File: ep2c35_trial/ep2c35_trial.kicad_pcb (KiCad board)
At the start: 4 copper layers, 70.4 x 57.6 mm, 139 parts, among them J1 Conn_02x21_Odd_Even, J2 Conn_02x21_Odd_Even, J3 3M_8540-4500PL, J4 USB3_B_Micro_Amphenol_GSB343K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, J5 Conn_02x05_Odd_Even, J6 Conn_01x02_Male, J7 Conn_01x02_Male, J8 Conn_01x02_Male, J9 Conn_01x02_Male, U1 EP2C5F484, U2 MIC37302, U3 FT600Q-B-T, U4 W25Q16JVSNIQ, U5 MIC39102, U6 MIC49150-1.2, X1 FNETHE025, Y1 ABM7-30.000MHZ-D2Y-T

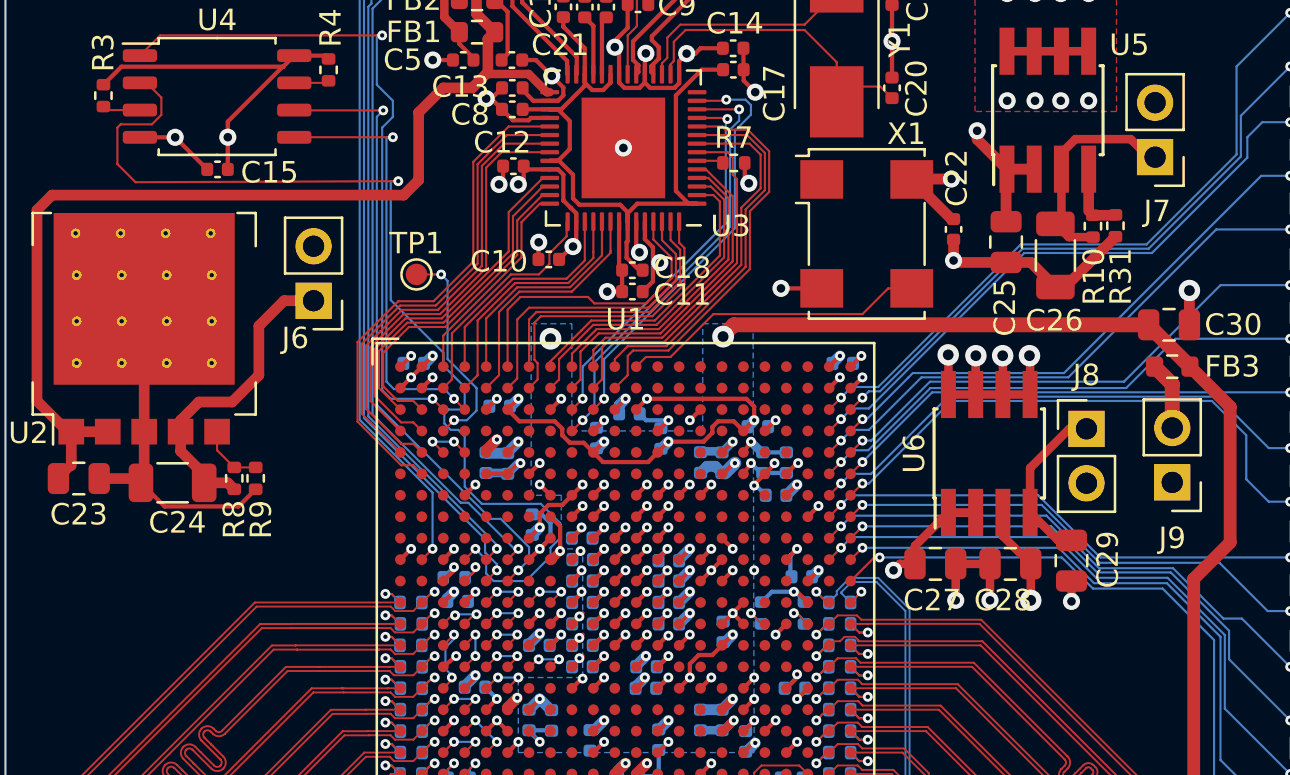
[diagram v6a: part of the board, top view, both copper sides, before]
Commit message: Create assembly file. WIP.
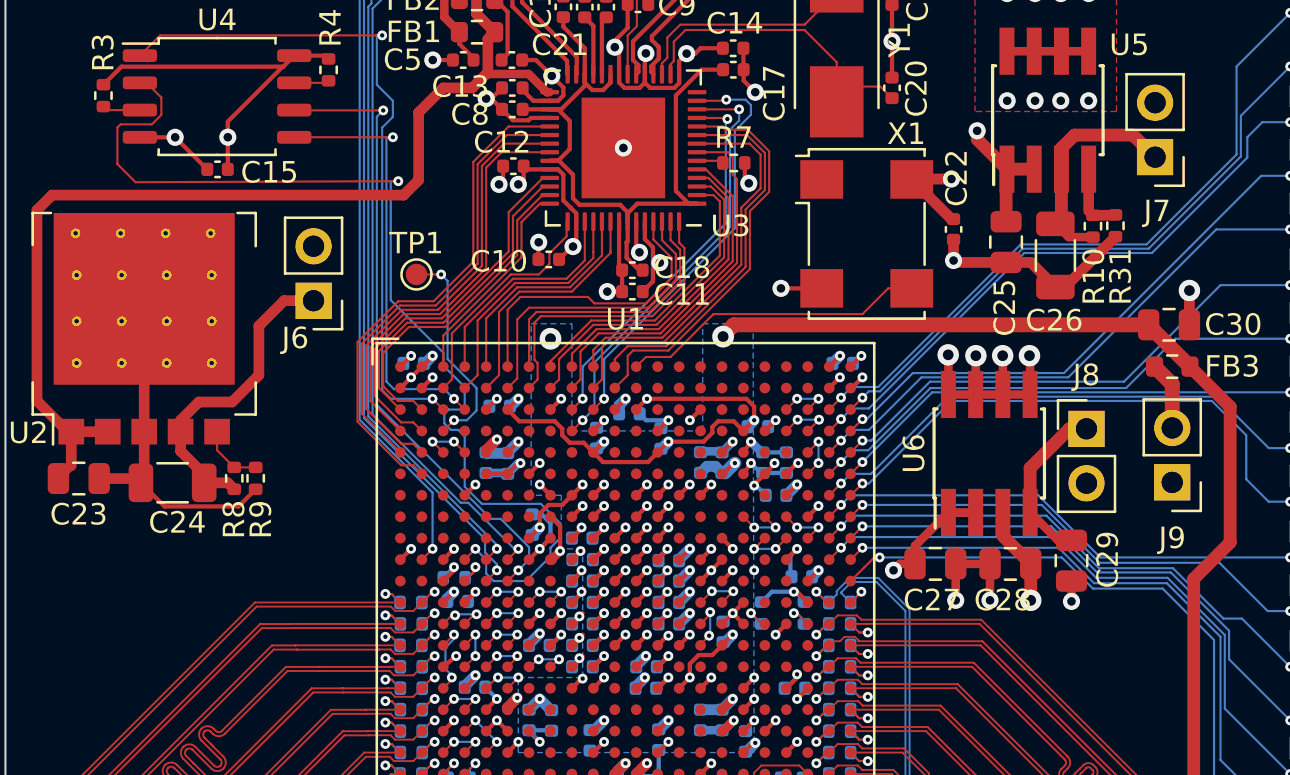
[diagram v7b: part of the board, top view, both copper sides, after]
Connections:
- U1 pad C19: unconnected-(U1-PadC19) -> /LVDS101
- U1 pad C20: unconnected-(U1-PadC20) -> /LVDS101
- U1 pad D19: unconnected-(U1-PadD19) -> /LVDS100
- U1 pad D20: unconnected-(U1-PadD20) -> /LVDS100
- U1 pad E20: unconnected-(U1-PadE20) -> /LVDS105
- U1 pad F20: unconnected-(U1-PadF20) -> /LVDS105
- U1 pad H17: unconnected-(U1-PadH17) -> /LVDS111
- U1 pad H18: unconnected-(U1-PadH18) -> /LVDS111
- U1 pad H19: unconnected-(U1-PadH19) -> /LVDS120
- U1 pad J18: unconnected-(U1-PadJ18) -> /LVDS117
- U1 pad J19: unconnected-(U1-PadJ19) -> /LVDS117
- U1 pad J20: unconnected-(U1-PadJ20) -> /LVDS120
- U1 pad M15: unconnected-(U1-PadM15) -> /LVDS130
- U1 pad M16: unconnected-(U1-PadM16) -> /LVDS130
- U1 pad N15: unconnected-(U1-PadN15) -> /LVDS132
- U1 pad P15: unconnected-(U1-PadP15) -> /LVDS132
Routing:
- net /LVDS105: track 0.00 -> 2.56 mm, vias 0 -> 2
- net /LVDS132: track 0.00 -> 2.54 mm, vias 0 -> 2
- net /LVDS130: track 0.00 -> 2.52 mm, vias 0 -> 2
- net /LVDS101: track 0.00 -> 2.51 mm, vias 0 -> 2
- net /LVDS100: track 0.00 -> 2.51 mm, vias 0 -> 2
- net /LVDS120: track 0.00 -> 2.48 mm, vias 0 -> 2
- net /LVDS117: track 0.00 -> 2.41 mm, vias 0 -> 2
- net /LVDS111: track 0.00 -> 2.41 mm, vias 0 -> 2
- net /2V5_LDO: track 10.1 -> 11.5 mm

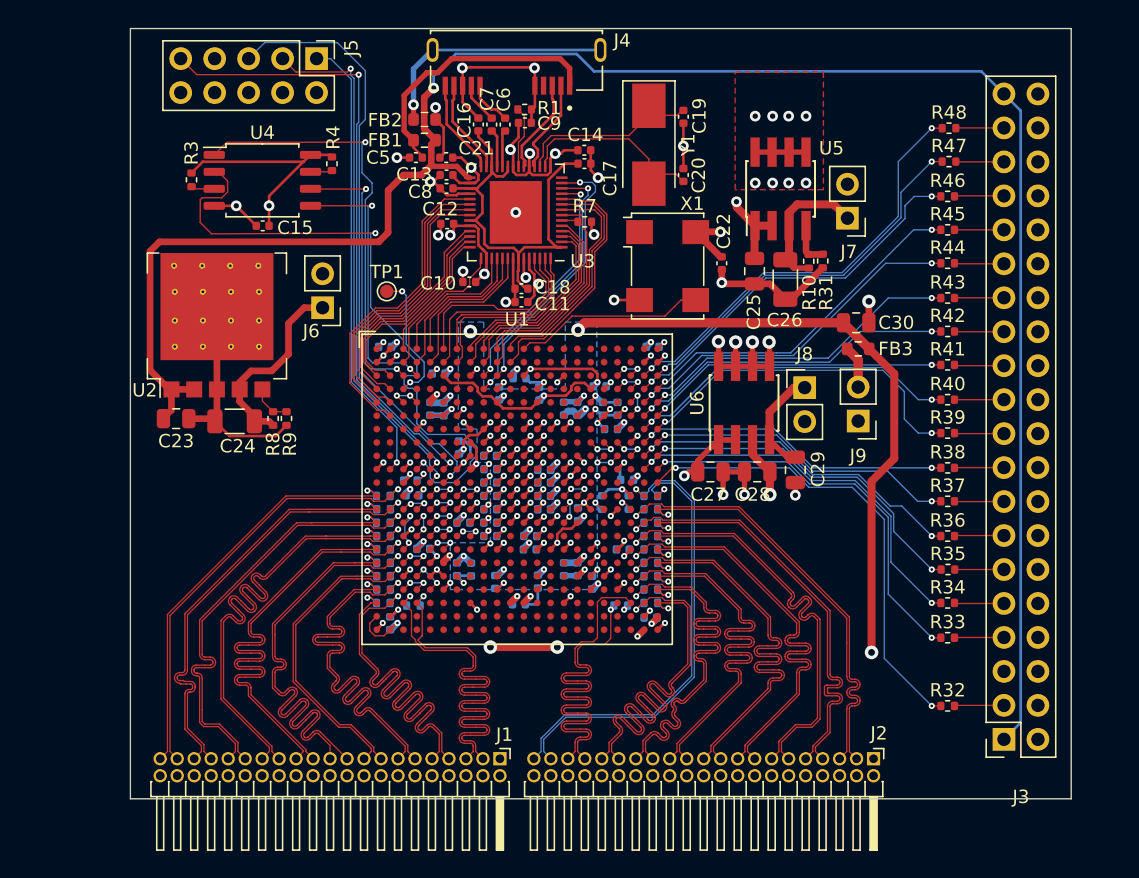
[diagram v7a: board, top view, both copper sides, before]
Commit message: Move JLCPCB components to bottom.
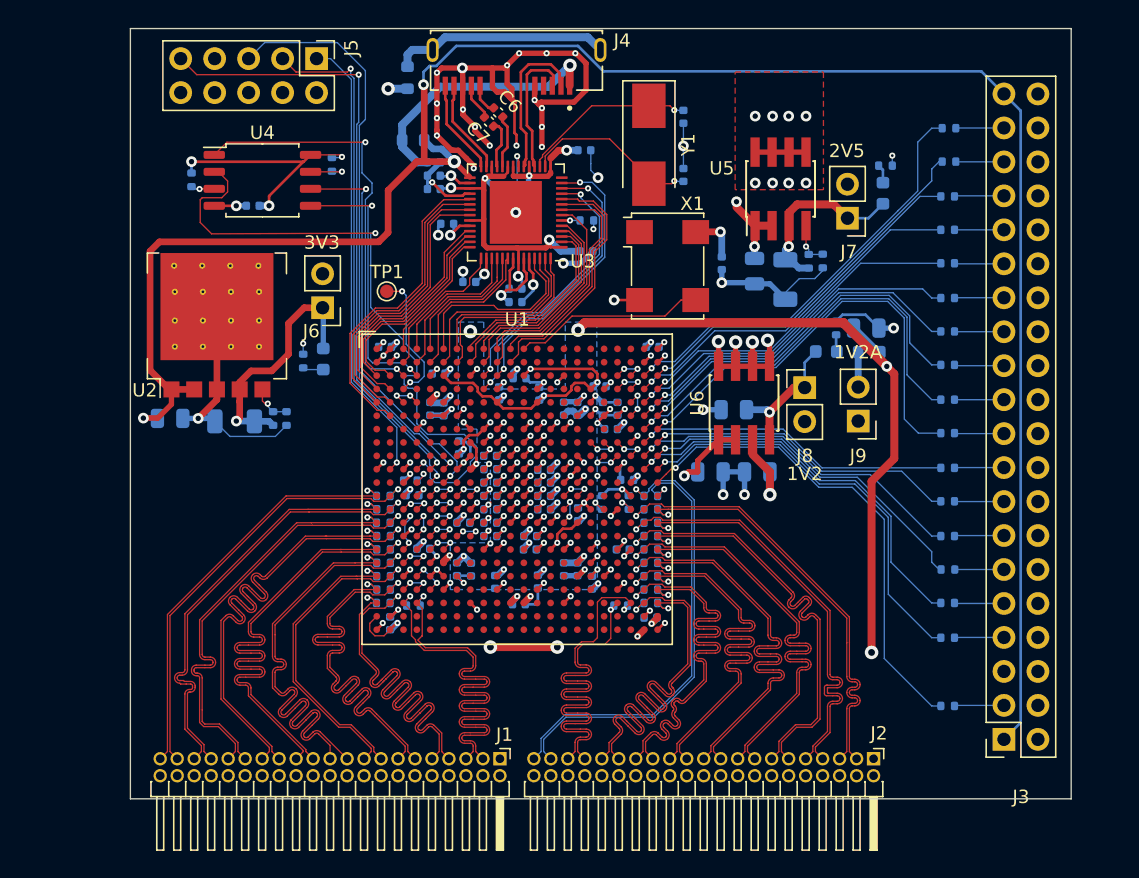
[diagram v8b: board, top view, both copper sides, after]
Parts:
- removed C21: 4.7u, Capacitor_SMD:C_0402_1005Metric
- added D1: LED, LED_SMD:LED_0603_1608Metric, B.Cu at (130.0, 71.8)
- added D2: LED, LED_SMD:LED_0603_1608Metric, B.Cu at (171.8, 59.4)
- added D3: LED, LED_SMD:LED_0603_1608Metric, B.Cu at (167.6, 71.2)
- added R49: 1k, Resistor_SMD:R_0402_1005Metric, B.Cu at (128.5, 71.9)
- added R50: 1k, Resistor_SMD:R_0402_1005Metric, B.Cu at (172.0, 57.3)
- added R51: 1k, Resistor_SMD:R_0402_1005Metric, B.Cu at (168.3, 69.4)
- C10, C11, C12, C13, C14, C15, C16, C17, C18, C19, C20, C22, C23, C24, C25, C26, C27, C28, C29, C30, C5, C8, C9, FB1, FB2, FB3, R1, R10, R31, R32, R33, R34, R35, R36, R37, R38, R39, R40, R41, R42, R43, R44, R45, R46, R47, R48, R7: moved to B.Cu
- R2, R5, R6: value 10K -> 10k
- R3, R4: value 10K -> 10k; moved to B.Cu
- R8: value 10k -> 5k; moved to B.Cu
- R9: value 10k -> 3k; moved to B.Cu
- moved C17 6.55 mm to (149.7, 63.7)
- moved C29 6.44 mm to (160.7, 75.5), turned to 0 degrees
- moved R1 6.35 mm to (144.3, 59.4), turned to -90 degrees
- moved C16 5.38 mm to (142.9, 59.4), turned to 90 degrees
- moved C9 5.29 mm to (145.3, 59.4), turned to 90 degrees
- moved FB2 3.38 mm to (136.3, 50.7), turned to -90 degrees
- moved C15 1.67 mm to (124.7, 60.3)
- moved C5 1.38 mm to (138.3, 57.0), turned to 0 degrees
- moved C6 1.05 mm to (143.1, 53.3), turned to -45 degrees
- moved C13 0.95 mm to (138.3, 58.0)
- moved C8 0.95 mm to (138.3, 59.0)
- moved FB3 0.86 mm to (170.8, 71.2)
- moved C30 0.85 mm to (170.6, 69.5)
- moved FB1 0.85 mm to (136.7, 55.4)
- moved C23 0.45 mm to (118.5, 76.2)
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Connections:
- U3 pad 18: /USB_D_N -> /USB_D_P
- U3 pad 20: /USB_D_P -> /USB_D_N
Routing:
- net GND: track 186.2 -> 232.5 mm, vias 108 -> 126
- net +3.3V: track 111.9 -> 104.2 mm, vias 30 -> 32
- net /DIG_D9: track 26.2 -> 33.6 mm, vias 2 -> 1
- net +1V0: track 33.5 -> 26.1 mm, vias 0 -> 4
- net /DIG_D8: track 25.1 -> 31.9 mm, vias 2 -> 1
- net /VBUS: track 145.3 -> 151.0 mm, vias 1 -> 3
- net /DIG_D7: track 22.8 -> 28.2 mm, vias 2 -> 1
- net /USB_D_N: track 7.20 -> 11.7 mm
- net +1V2A: track 62.1 -> 66.1 mm, vias 9 -> 10
- net /3V3_LDO: track 14.9 -> 18.8 mm, vias 0 -> 1
- net /2V5_LDO: track 11.5 -> 14.5 mm, vias 0 -> 1
- net /USB_D_P: track 7.21 -> 10.2 mm
- net /DIG_D6: track 24.8 -> 27.2 mm, vias 2 -> 1
- net /1V2_LDO: track 7.93 -> 10.3 mm, vias 0 -> 1
- net /USB_SHIELD: track 18.3 -> 16.3 mm, vias 1 -> 0
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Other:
- board text added: "1V2"
- board text added: "1V2A"
- board text added: "2V5"
- board text added: "3V3"
